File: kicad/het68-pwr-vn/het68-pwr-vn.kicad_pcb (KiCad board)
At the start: 2 copper layers, 140 x 80 mm, 65 parts, among them J1 CT_SEC, J2 USB_C, J3 VOUT, Q1 X0202MN, Q2 AO3400A, Q3 AO3401A, Q4 AO3400A

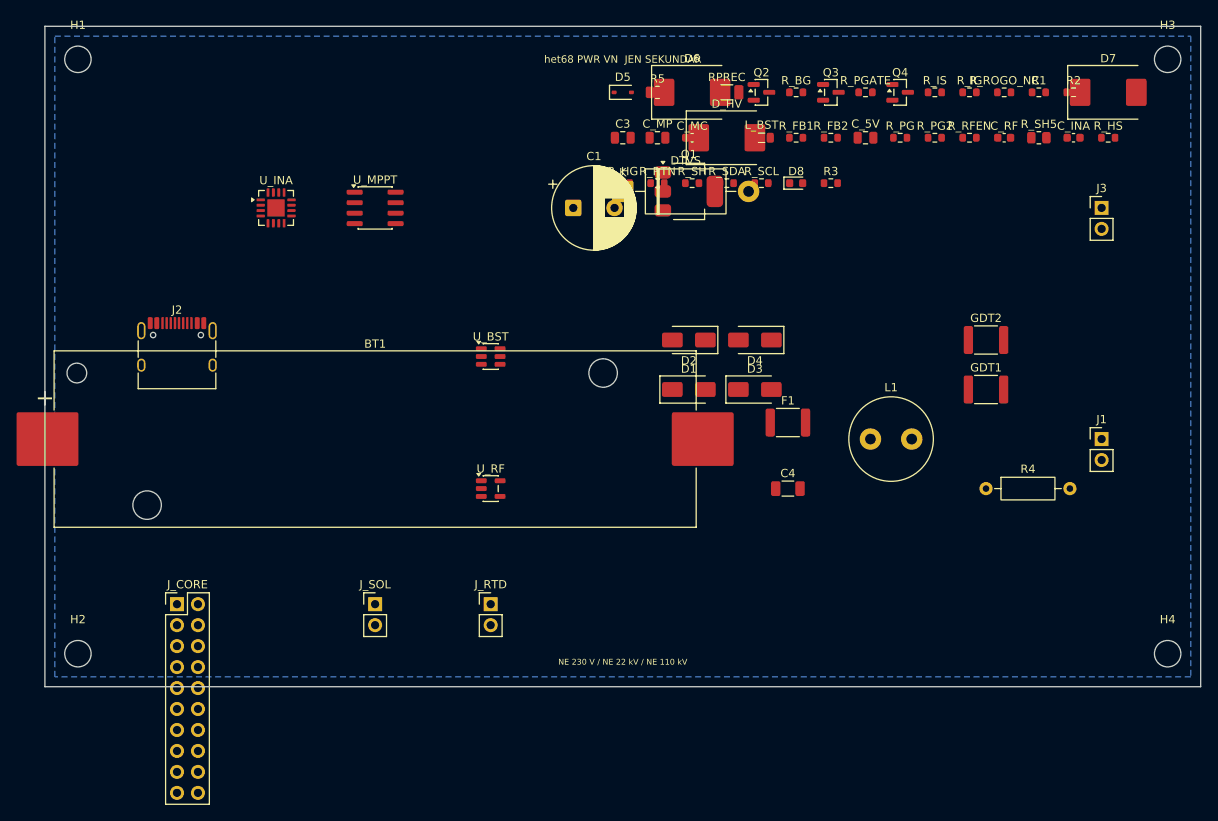
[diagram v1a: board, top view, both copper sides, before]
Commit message: Add a Core status LED and three buttons, and fit a 21700 holder.
RESET, BOOT and USER sit on the east edge with one SK6812; the power board uses a Keystone 1122 instead of an 18650 sled. Masks, schematics and JLCPCB gerber zips are in the tree.

Co-authored-by: Cursor <cursoragent@cursor.com>
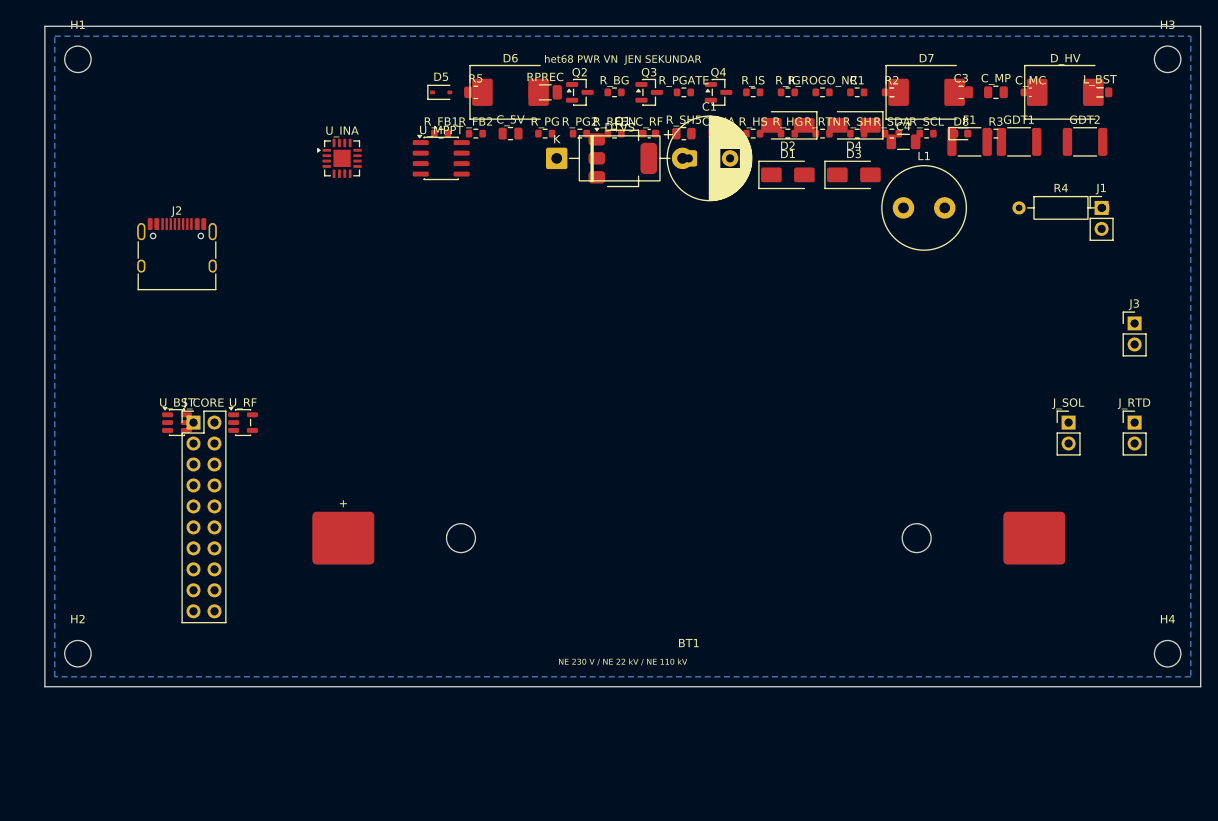
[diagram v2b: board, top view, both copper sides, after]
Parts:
- BT1: value LiFePO4_1S -> 21700; footprint Battery:BatteryHolder_Keystone_1042_1x18650 -> het68:Keystone_1122_21700
- moved J_SOL 86.8 mm to (124.0, 48.0)
- moved J_RTD 81.0 mm to (132.0, 48.0)
- moved C4 44.3 mm to (104.0, 14.0)
- moved R_HS 43.0 mm to (85.8, 13.0)
- moved C_5V 43.0 mm to (56.4, 13.0)
- moved C_INA 43.0 mm to (81.6, 13.0)
- moved C_RF 43.0 mm to (73.2, 13.0)
- moved R_FB1 43.0 mm to (48.0, 13.0)
- moved R_FB2 43.0 mm to (52.2, 13.0)
- moved R_PG2 43.0 mm to (64.8, 13.0)
- moved R_RFEN 43.0 mm to (69.0, 13.0)
- moved R_SH5 43.0 mm to (77.4, 13.0)
- moved R_PG 43.0 mm to (60.6, 13.0)
- moved C3 41.4 mm to (111.0, 8.00)
- moved C_MC 41.4 mm to (119.4, 8.00)
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
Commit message: Route signal copper on the five v4 boards and drop tracks that still short.
Core and the satellite have no copper shorts left. QFN-80 fanout and a few LVDS pairs stay open, and the power boards still have overlapping pads from placement.

Co-authored-by: Cursor <cursoragent@cursor.com>
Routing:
- net SOL_P: track 0.00 -> 150.3 mm, vias 0 -> 4
- net CC1: track 0.00 -> 104.6 mm
- net PG_5V: track 0.00 -> 103.8 mm
- net EN_RF: track 0.00 -> 102.6 mm, vias 0 -> 1
- net CC2: track 0.00 -> 100.6 mm, vias 0 -> 2
- net MPPT_C: track 0.00 -> 88.2 mm, vias 0 -> 2
- net BST_FB: track 0.00 -> 78.4 mm, vias 0 -> 2
- net I2C0_ALERT: track 0.00 -> 72.3 mm
- net SCR_G: track 0.00 -> 58.2 mm
- net 5V_IN: track 0.00 -> 50.0 mm
- net VHARV: track 0.00 -> 49.3 mm, vias 0 -> 4
- net GND: track 0.00 -> 44.6 mm, vias 0 -> 34
- net AC1F: track 0.00 -> 32.0 mm, vias 0 -> 2
- net CHG_G: track 0.00 -> 19.1 mm
- net AC1L: track 0.00 -> 15.7 mm
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
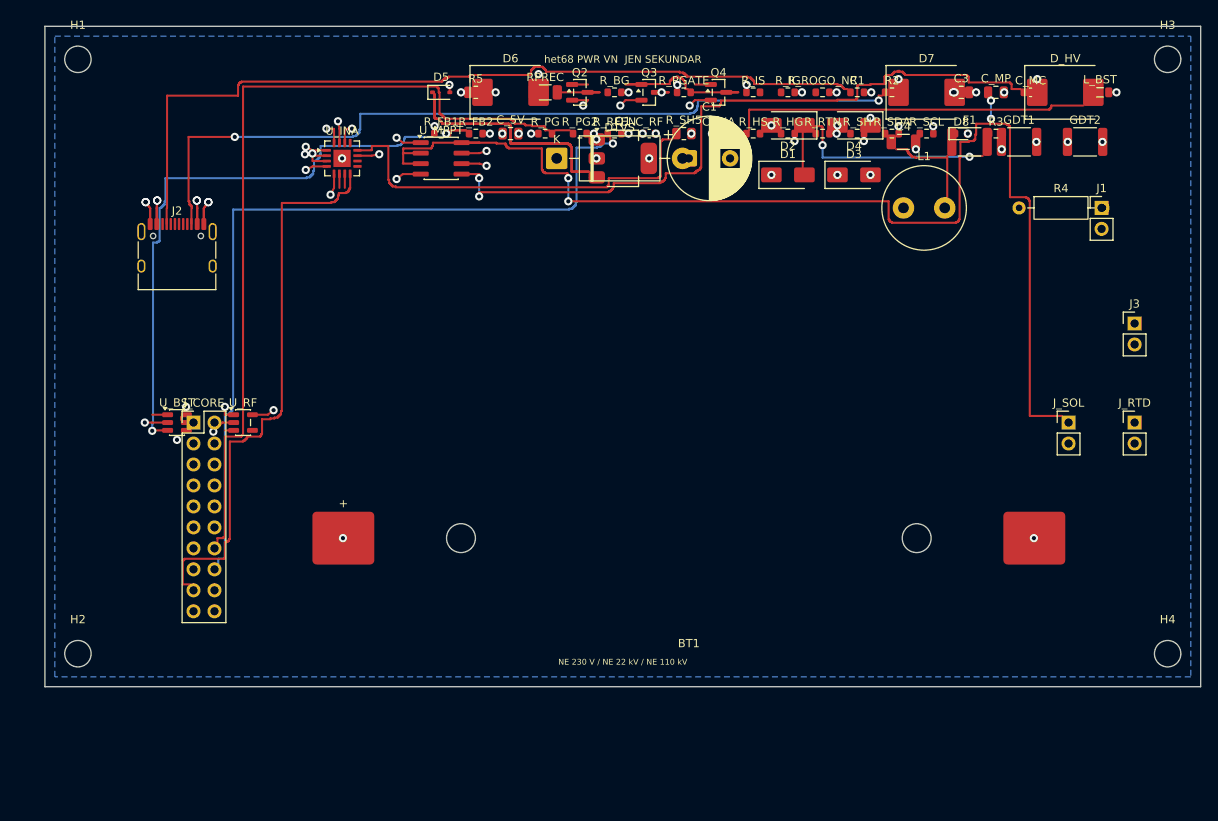
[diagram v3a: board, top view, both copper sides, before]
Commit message: Fan out the RP2350B and finish the signal bridges that can leave the package.
Each QFN pin gets a 0.15 mm escape along its axis. The crystal moves off the north row so that corridor exists. Core and the satellite have no new shorts; a few center-row pins and some LVDS nets are still open.

Co-authored-by: Cursor <cursoragent@cursor.com>
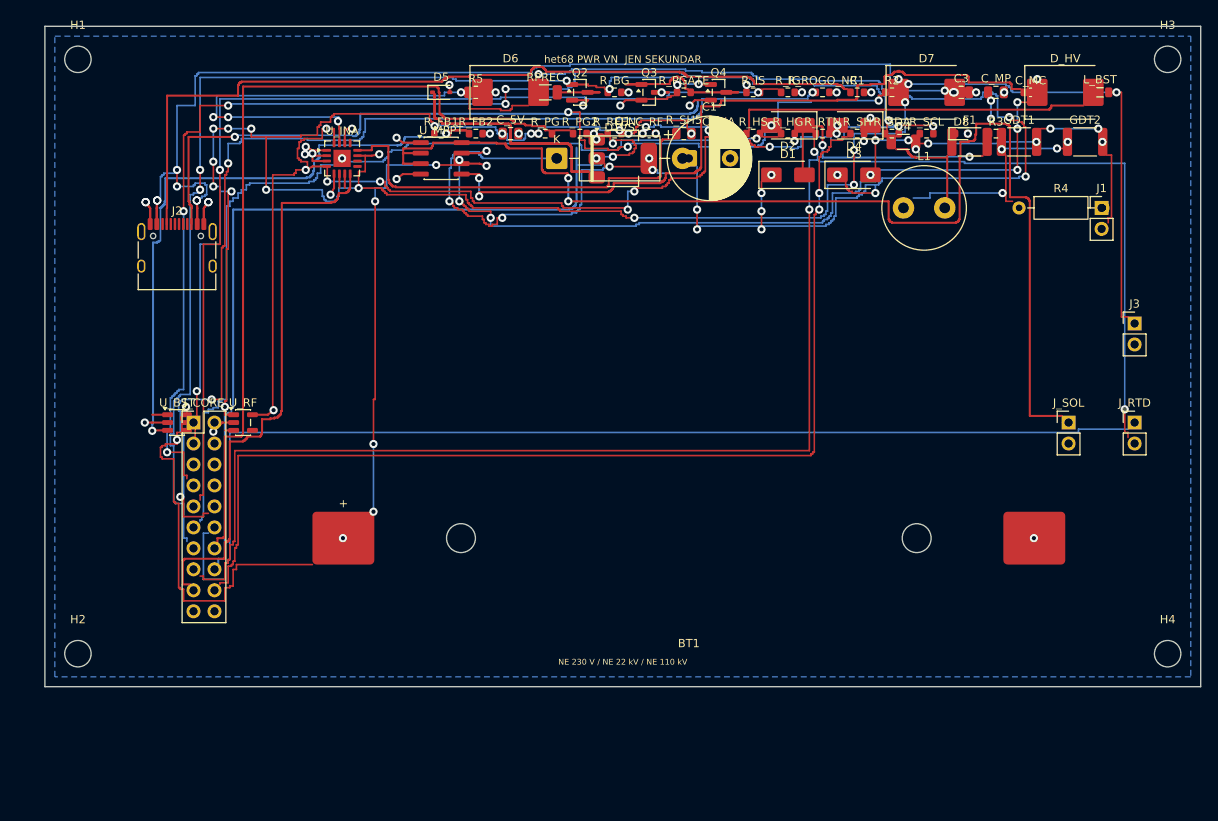
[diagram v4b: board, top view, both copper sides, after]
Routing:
- net +5V_ALWAYS: track 8.25 -> 306.7 mm, vias 9 -> 25
- net DC: track 8.18 -> 269.6 mm, vias 10 -> 24
- net PT1000_RTN: track 1.39 -> 201.8 mm, vias 0 -> 3
- net BAT: track 6.53 -> 198.3 mm, vias 6 -> 16
- net I2C0_SDA: track 3.10 -> 149.3 mm, vias 0 -> 6
- net +3V3_RF: track 9.83 -> 152.6 mm, vias 7 -> 14
- net ADC_PT1000: track 1.39 -> 137.8 mm
- net ADC_ROGO: track 1.39 -> 134.8 mm, vias 0 -> 4
- net SHIELD: track 1.39 -> 131.6 mm, vias 0 -> 2
- net VBUS: track 11.4 -> 136.0 mm, vias 6 -> 9
- net BURDEN_EN: track 5.27 -> 127.7 mm, vias 0 -> 5
- net ADC_I: track 1.39 -> 120.6 mm, vias 0 -> 2
- net ADC_HARVEST: track 1.39 -> 119.0 mm, vias 0 -> 1
- net AC2: track 4.62 -> 43.8 mm, vias 6 -> 11
- net CC2: track 100.6 -> 127.9 mm, vias 2 -> 4
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
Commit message: Put the satellite electronics on the back and clear the power-board pad shorts.
The outward face keeps only the microphone hole and the eight SK6812s. The DO-201 and the two regulators move off the header so the power boards no longer short pad to pad. Some LVDS, QSPI and GPIO nets are still open.

Co-authored-by: Cursor <cursoragent@cursor.com>
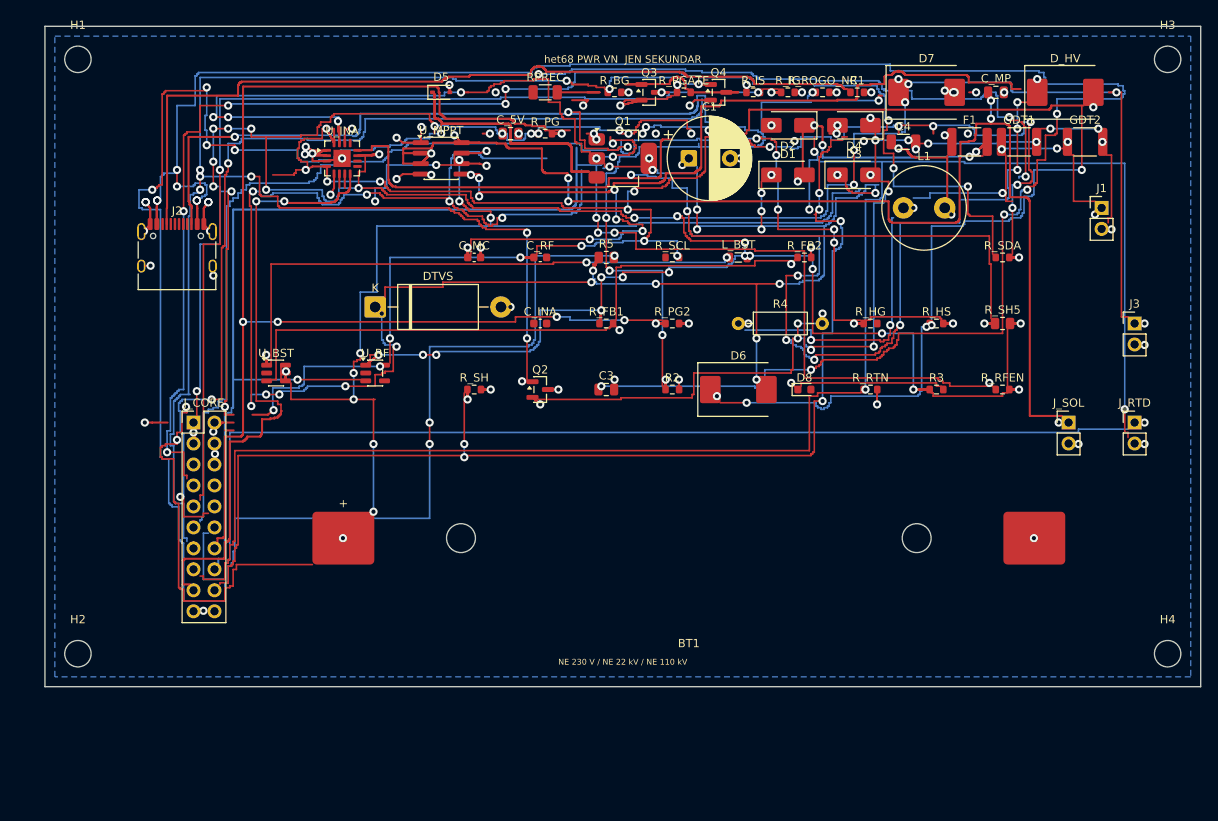
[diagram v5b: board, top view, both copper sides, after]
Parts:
- moved C_MC 70.3 mm to (52.0, 28.0)
- moved R_RFEN 56.3 mm to (116.0, 44.0)
- moved C3 56.1 mm to (68.0, 44.0)
- moved R_SH 55.8 mm to (52.0, 44.0)
- moved L_BST 48.2 mm to (84.0, 28.0)
- moved D6 45.4 mm to (84.0, 44.0)
- moved R_SH5 44.9 mm to (116.0, 36.0)
- moved R2 44.8 mm to (76.0, 44.0)
- moved R_FB2 42.5 mm to (92.0, 28.0)
- moved R4 36.8 mm to (84.0, 36.0)
- moved D8 36.4 mm to (92.0, 44.0)
- moved Q2 36.3 mm to (60.0, 44.0)
- moved R_SCL 34.3 mm to (76.0, 28.0)
- moved R_HS 32.0 mm to (108.0, 36.0)
- moved R3 31.8 mm to (108.0, 44.0)
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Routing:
- net SCR_G: track 58.2 -> 270.4 mm, vias 0 -> 8
- net DC: track 269.6 -> 471.8 mm, vias 24 -> 39
- net +5V_ALWAYS: track 306.7 -> 504.4 mm, vias 25 -> 43
- net VBUS: track 136.0 -> 326.0 mm, vias 9 -> 14
- net GND: track 44.6 -> 171.1 mm, vias 34 -> 53
- net +3V3_RF: track 152.6 -> 274.4 mm, vias 14 -> 24
- net BAT: track 198.3 -> 301.6 mm, vias 16 -> 24
- net EN_RF: track 111.1 -> 202.1 mm, vias 2 -> 7
- net AC2: track 43.8 -> 131.7 mm, vias 11 -> 19
- net VHARV: track 49.3 -> 133.4 mm, vias 4 -> 10
- net BURDEN_EN: track 127.7 -> 202.9 mm, vias 5 -> 10
- net BST_SW: track 1.86 -> 76.8 mm, vias 0 -> 3
- net 5V_IN: track 50.0 -> 119.8 mm, vias 0 -> 3
- net PG_5V: track 103.8 -> 171.8 mm, vias 0 -> 6
- net ADC_HARVEST: track 119.0 -> 181.0 mm, vias 1 -> 7
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
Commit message: Ship the furthest routed v4 boards with matching previews.
The satellite signal nets are closed, the five boards have no shorts, and the gerbers and renders follow this copper.

Co-authored-by: Cursor <cursoragent@cursor.com>
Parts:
- moved J_SOL 2.95 mm to (127.0, 48.0)
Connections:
- J2 pad A6: unconnected-(J2-D+-PadA6) -> (no net)
- J2 pad A7: unconnected-(J2-D--PadA7) -> (no net)
- J2 pad A8: unconnected-(J2-SBU1-PadA8) -> (no net)
- J2 pad B6: unconnected-(J2-D+-PadB6) -> (no net)
- J2 pad B7: unconnected-(J2-D--PadB7) -> (no net)
- J2 pad B8: unconnected-(J2-SBU2-PadB8) -> (no net)
- U_INA pad 10: unconnected-(U_INA-PV-Pad10) -> (no net)
- U_INA pad 13: unconnected-(U_INA-TC-Pad13) -> (no net)
- U_INA pad 9: unconnected-(U_INA-CRITICAL-Pad9) -> (no net)
- U_RF pad 4: unconnected-(U_RF-NC-Pad4) -> (no net)
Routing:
- net GND: track 171.1 -> 295.6 mm, vias 53 -> 55
- net ADC_PT1000: track 139.0 -> 146.1 mm, vias 1 -> 2
- net AC1: track 72.8 -> 77.5 mm, vias 9 -> 12
- net SOL_P: track 172.2 -> 175.9 mm
- net PT1000_RTN: track 216.6 -> 219.3 mm
- net ADC_ROGO: track 122.0 -> 123.6 mm
- net ADC_I: track 128.8 -> 130.4 mm
- net BURDEN_EN: track 202.9 -> 204.4 mm, vias 10 -> 11
- net I2C0_SDA: track 177.9 -> 179.4 mm
- net DC: track 471.8 -> 473.2 mm, vias 39 -> 40
- net ADC_HARVEST: track 181.0 -> 182.2 mm, vias 7 -> 8
- net SHIELD: track 154.6 -> 155.7 mm
- net AC2: track 131.7 -> 132.8 mm
